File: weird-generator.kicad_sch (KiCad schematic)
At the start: 66 parts, among them J1 Battery Connector, J2 Audio Out, Q1 2N3904, Q2 2N3904, SW1 Unusual, SW2 Unusual, SW3 Wacky, SW4 Wacky, SW5 Wacky Out, SW6 Wacky Out, SW7 ON/OFF, U1 40106, U3 LM741

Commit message: Initial PCB iteration
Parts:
- RV1, RV10, RV11, RV2, RV3, RV4, RV5, RV6, RV7, RV8, RV9: footprint Potentiometer_THT:Potentiometer_Omeg_PC16BU_Vertical -> fx_synth_parts:potentiometer_fx_vertical
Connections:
- net -BATT: now reaches RV6.3
- net -BATT: now also C1.2, C10.2, C11.2, C13.2, C2.2, C3.2, C4.2, C7.2, C8.2, C9.2, J1.1 (Pin_1), J2.2 (Pin_2), R17.2, R20.2, RV5.3, SW1.2 (B), SW2.2 (B), U1.7 (VSS), U3.4 (V-)
- net +BATT: now reaches C10.1, C9.1
- net +BATT: now also C11.1, SW7.2 (B), U1.14 (VDD), U3.7 (V+)

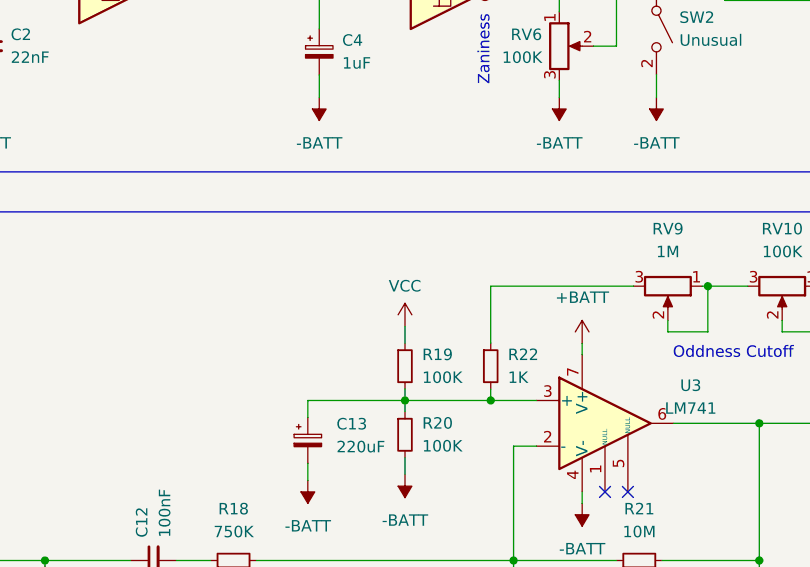
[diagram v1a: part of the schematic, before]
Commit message: Completed trace routing
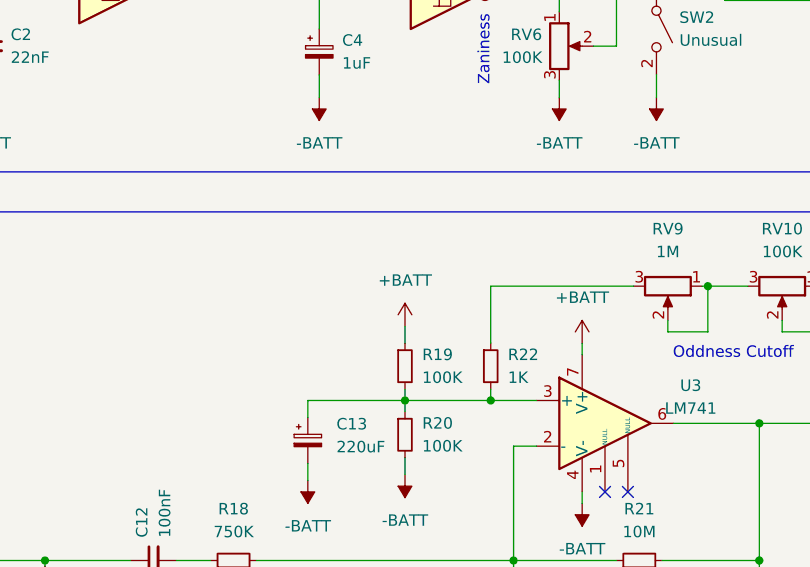
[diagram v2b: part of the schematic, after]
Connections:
- net +BATT: now also R19.1
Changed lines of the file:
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@@
+    (stroke (width 0) (type default))
+  )
+  (wire (pts (xy 29.21 34.925) (xy 31.115 34.925))
+    (stroke (width 0) (type default))
+  )
+  (wire (pts (xy 140.97 96.52) (xy 142.875 96.52))
+    (stroke (width 0) (type default))
+  )
+  (wire (pts (xy 158.115 110.49) (xy 164.465 110.49))
+    (stroke (width 0) (type default))
+  )
+  (wire (pts (xy 113.665 150.495) (xy 118.11 150.495))
+    (stroke (width 0) (type default))
+  )
+  (wire (pts (xy 184.785 107.95) (xy 184.785 110.49))
+    (stroke (width 0) (type default))
+  )
+  (wire (pts (xy 137.795 46.355) (xy 137.795 48.895))
+    (stroke (width 0) (type default))
+  )
+  (wire (pts (xy 71.755 156.845) (xy 71.755 158.115))
+    (stroke (width 0) (type default))
+  )
+  (wire (pts (xy 111.125 182.245) (xy 111.125 183.515))
+    (stroke (width 0) (type default))
+  )
+  (wire (pts (xy 71.755 164.465) (xy 71.755 166.37))
+    (stroke (width 0) (type default))
+  )
+  (wire (pts (xy 31.115 29.21) (xy 31.115 34.925))
     (stroke (width 0) (type default))
   )
   (wire (pts (xy 71.755 149.86) (xy 71.755 151.765))
-    (stroke (width 0) (type default))
-  )
-  (wire (pts (xy 29.21 34.925) (xy 31.115 34.925))
-    (stroke (width 0) (type default))
-  )
-  (wire (pts (xy 140.97 96.52) (xy 142.875 96.52))
-    (stroke (width 0) (type default))
-  )
-  (wire (pts (xy 158.115 110.49) (xy 164.465 110.49))
-    (stroke (width 0) (type default))
-  )
-  (wire (pts (xy 113.665 150.495) (xy 118.11 150.495))
-    (stroke (width 0) (type default))
-  )
-  (wire (pts (xy 184.785 107.95) (xy 184.785 110.49))
-    (stroke (width 0) (type default))
-  )
-  (wire (pts (xy 137.795 46.355) (xy 137.795 48.895))
-    (stroke (width 0) (type default))
-  )
-  (wire (pts (xy 71.755 156.845) (xy 71.755 158.115))
-    (stroke (width 0) (type default))
-  )
-  (wire (pts (xy 111.125 182.245) (xy 111.125 183.515))
-    (stroke (width 0) (type default))
-  )
-  (wire (pts (xy 71.755 164.465) (xy 71.755 166.37))
-    (stroke (width 0) (type default))
-  )
-  (wire (pts (xy 31.115 29.21) (xy 31.115 34.925))
     (stroke (width 0) (type default))
   )
@@
         (path "/8f901d28-4cca-4344-9d90-845b9140dffb"
           (reference "R9") (unit 1)
+        )
+      )
+    )
+  )
+  (symbol (lib_id "power:+BATT") (at 71.755 149.86 0) (unit 1)
+    (in_bom yes) (on_board yes) (dnp no) (fields_autoplaced)
+    (property "Reference" "#PWR019" (at 71.755 153.67 0)
+      (effects (font (size 1.27 1.27)) hide)
+    )
+    (property "Value" "+BATT" (at 71.755 144.78 0)
+      (effects (font (size 1.27 1.27)))
+    )
+    (property "Footprint" "" (at 71.755 149.86 0)
+      (effects (font (size 1.27 1.27)) hide)
+    )
+    (property "Datasheet" "" (at 71.755 149.86 0)
+      (effects (font (size 1.27 1.27)) hide)
+    )
+    (pin "1")
+    (instances
+      (project "weird-generator"
+        (path "/8f901d28-4cca-4344-9d90-845b9140dffb"
+          (reference "#PWR019") (unit 1)
         )
       )
@@
         )
       )
-    )
-  )
-  (symbol (lib_id "power:VCC") (at 71.755 149.86 0) (unit 1)
-    (in_bom yes) (on_board yes) (dnp no) (fields_autoplaced)
-    (property "Reference" "#PWR019" (at 71.755 153.67 0)
-      (effects (font (size 1.27 1.27)) hide)
-    )
-    (property "Value" "VCC" (at 71.755 145.415 0)
-      (effects (font (size 1.27 1.27)))
-    )
-    (property "Footprint" "" (at 71.755 149.86 0)
-      (effects (font (size 1.27 1.27)) hide)
-    )
-    (property "Datasheet" "" (at 71.755 149.86 0)
-      (effects (font (size 1.27 1.27)) hide)
-    )
-    (instances
-      (project "weird-generator"
-        (path "/8f901d28-4cca-4344-9d90-845b9140dffb"
-          (reference "#PWR019") (unit 1)
-        )
-      )

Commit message: Rearranged components and shrunk board
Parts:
- SW1, SW2, SW3, SW4, SW5, SW6, SW7: footprint Connector_PinHeader_2.54mm:PinHeader_1x03_P2.54mm_Vertical -> fx_synth_parts:switch_fx_connector
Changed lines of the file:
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@@
       (effects (font (size 1.27 1.27)) (justify left))
     )
-    (property "Footprint" "Connector_PinHeader_2.54mm:PinHeader_1x03_P2.54mm_Vertical" (at 117.475 95.885 0)
+    (property "Footprint" "fx_synth_parts:switch_fx_connector" (at 117.475 95.885 0)
       (effects (font (size 1.27 1.27)) hide)
     )
@@
       (effects (font (size 1.27 1.27)) (justify left))
     )
-    (property "Footprint" "Connector_PinHeader_2.54mm:PinHeader_1x03_P2.54mm_Vertical" (at 99.695 54.61 0)
+    (property "Footprint" "fx_synth_parts:switch_fx_connector" (at 99.695 54.61 0)
       (effects (font (size 1.27 1.27)) hide)
     )
@@
       (effects (font (size 1.27 1.27)))
     )
-    (property "Footprint" "Connector_PinHeader_2.54mm:PinHeader_1x03_P2.54mm_Vertical" (at 183.515 86.36 0)
+    (property "Footprint" "fx_synth_parts:switch_fx_connector" (at 183.515 86.36 0)
       (effects (font (size 1.27 1.27)) hide)
     )
@@
       (effects (font (size 1.27 1.27)) (justify left))
     )
-    (property "Footprint" "Connector_PinHeader_2.54mm:PinHeader_1x03_P2.54mm_Vertical" (at 118.11 34.29 0)
+    (property "Footprint" "fx_synth_parts:switch_fx_connector" (at 118.11 34.29 0)
       (effects (font (size 1.27 1.27)) hide)
     )
@@
       (effects (font (size 1.27 1.27)))
     )
-    (property "Footprint" "Connector_PinHeader_2.54mm:PinHeader_1x03_P2.54mm_Vertical" (at 255.27 103.505 0)
+    (property "Footprint" "fx_synth_parts:switch_fx_connector" (at 255.27 103.505 0)
       (effects (font (size 1.27 1.27)) hide)
     )
@@
       (effects (font (size 1.27 1.27)))
     )
-    (property "Footprint" "Connector_PinHeader_2.54mm:PinHeader_1x03_P2.54mm_Vertical" (at 184.15 24.765 0)
+    (property "Footprint" "fx_synth_parts:switch_fx_connector" (at 184.15 24.765 0)
       (effects (font (size 1.27 1.27)) hide)
     )
@@
       (effects (font (size 1.27 1.27)) (justify left))
     )
-    (property "Footprint" "Connector_PinHeader_2.54mm:PinHeader_1x03_P2.54mm_Vertical" (at 99.695 116.84 0)
-      (effects (font (size 1.27 1.27)) hide)
-    )
+    (property "Footprint" "fx_synth_parts:switch_fx_connector" (at 99.695 116.84 0)
+      (effects (font (size 1.27 1.27)) hide)
+    )

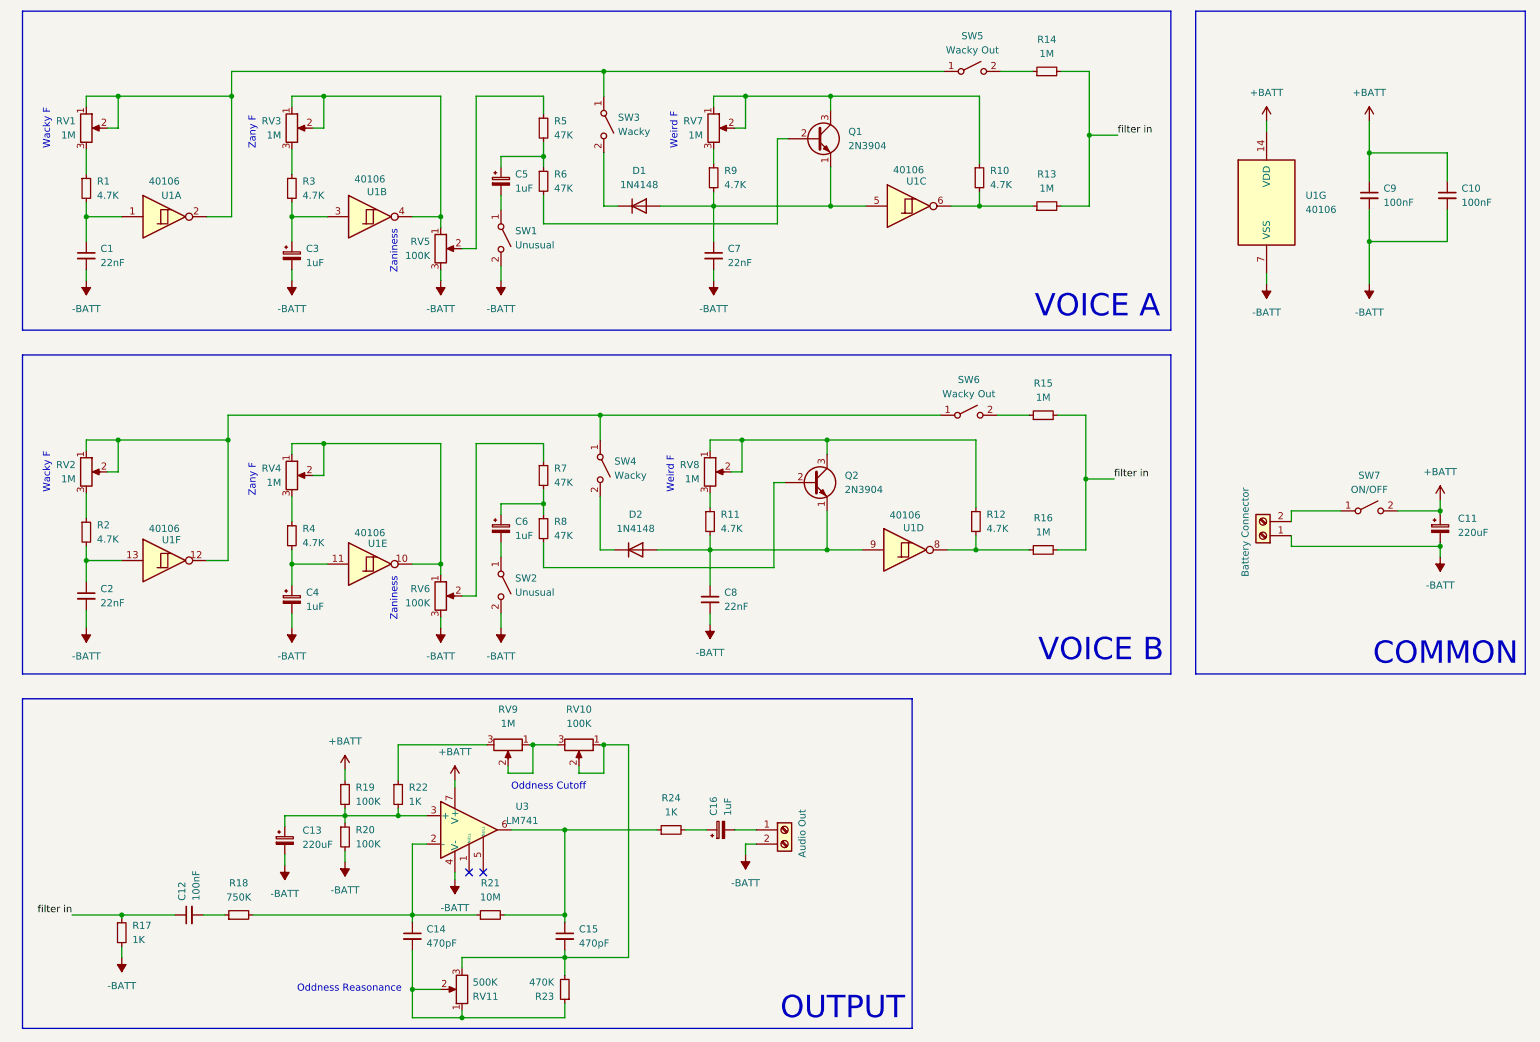
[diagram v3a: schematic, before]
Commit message: Redesigned to accommodate extra functionality
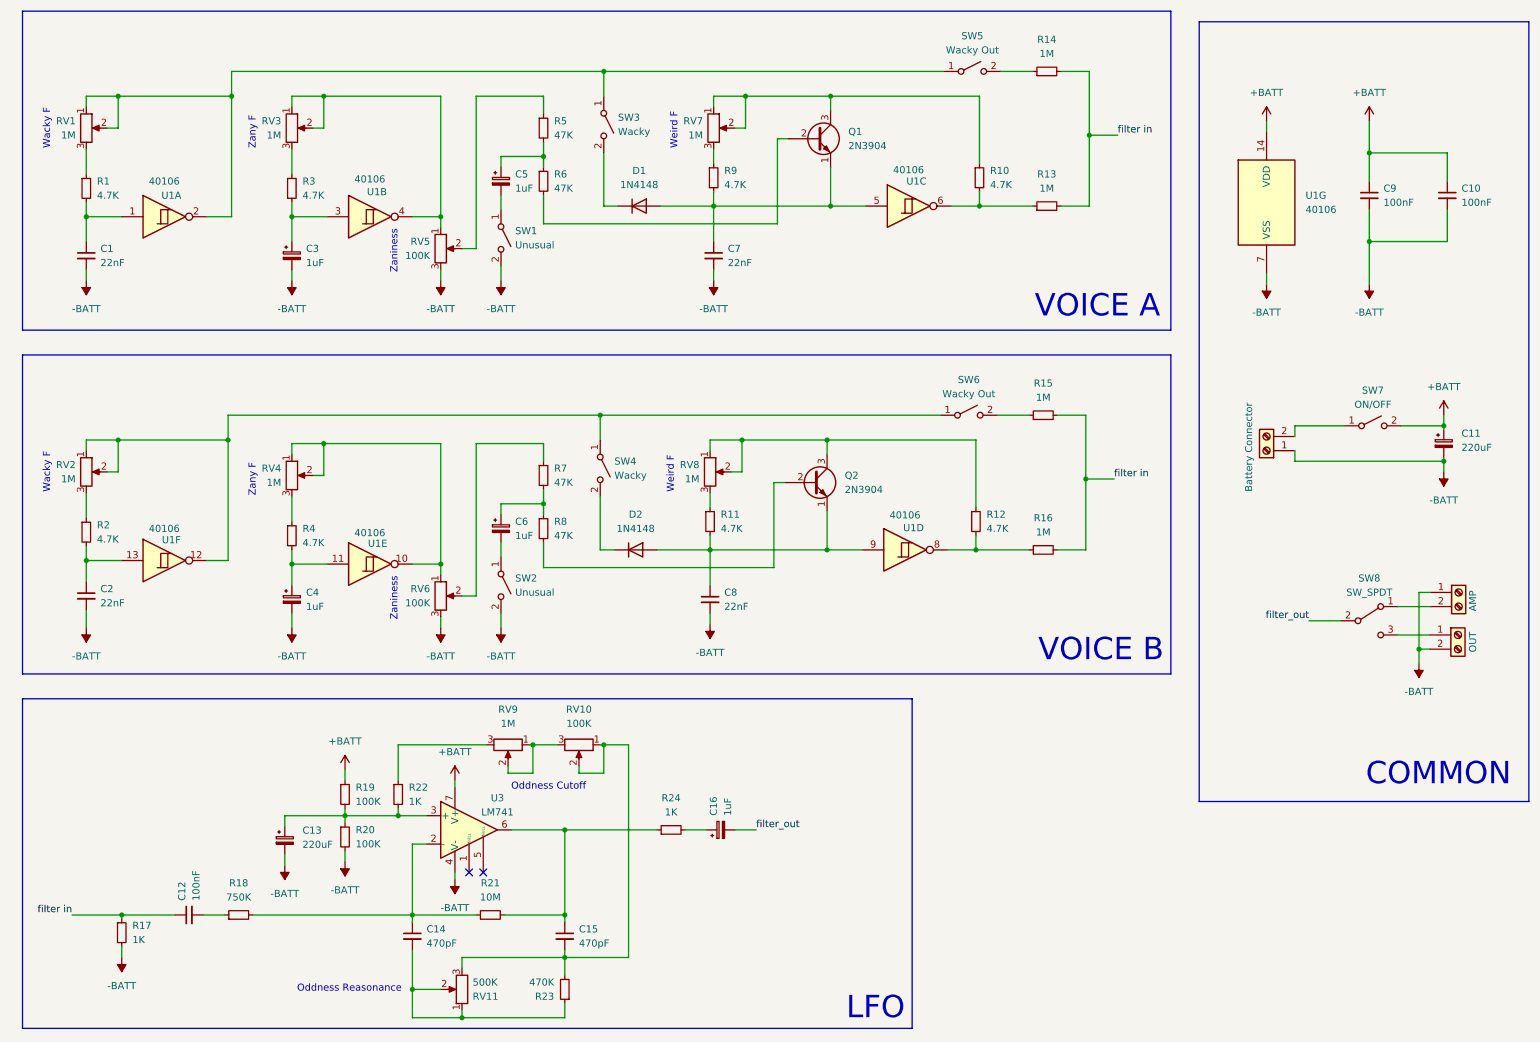
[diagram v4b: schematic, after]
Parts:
- added J3: AMP, TerminalBlock_Phoenix:TerminalBlock_Phoenix_MKDS-1,5-2_1x02_P5.00mm_Horizontal, symbol Connector:Screw_Terminal_01x02
- added SW8: SW_SPDT, fx_synth_parts:switch_fx_connector, symbol Switch:SW_SPDT
- J2: value Audio Out -> OUT
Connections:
- net -BATT: now also J3.1 (Pin_1)
- net at J2.1 (Pin_1): now also SW8.3 (C); no longer C16.2
- new net: J3.2 (Pin_2), SW8.1 (A)
- new net filter_out: C16.2, SW8.2 (B)
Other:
- note added: "LFO"
- note removed: "OUTPUT"
- moved on the sheet: C11, SW7
